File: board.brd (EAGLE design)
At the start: 76 x 83.5 mm, 82 parts, among them IC1 REG1117F, J1 LHBEAMOUT, J10 TEMP, J11 HORNOUT, J12 12V_SUPPLY, J13 STOPOUT, J14 TURNOUT, J15 FANOUT, J16 BLIGHTOUT, J17 AUXOUT, J18 AUX, J19 CAN, J2 BATT, J3 BLIGHT, J4 LHBEAM, J5 LRTURN, J6 WARNING, J7 HORN, J9 BREAK, Q1 FQD19N10LTM, Q2 FQD19N10LTM, Q3 FQD19N10LTM, Q4 IRF7424TRPBF, Q5 IRF7424TRPBF, Q6 IRF7424TRPBF, Q7 IRF7424TRPBF, Q8 IRF7424TRPBF, Q9 IRF7424TRPBF, U1 VOM1271T, U2 VOM1271T, U3 VOM1271T, U4 MC14504BDR2G, U5 MAX3051ESA+T

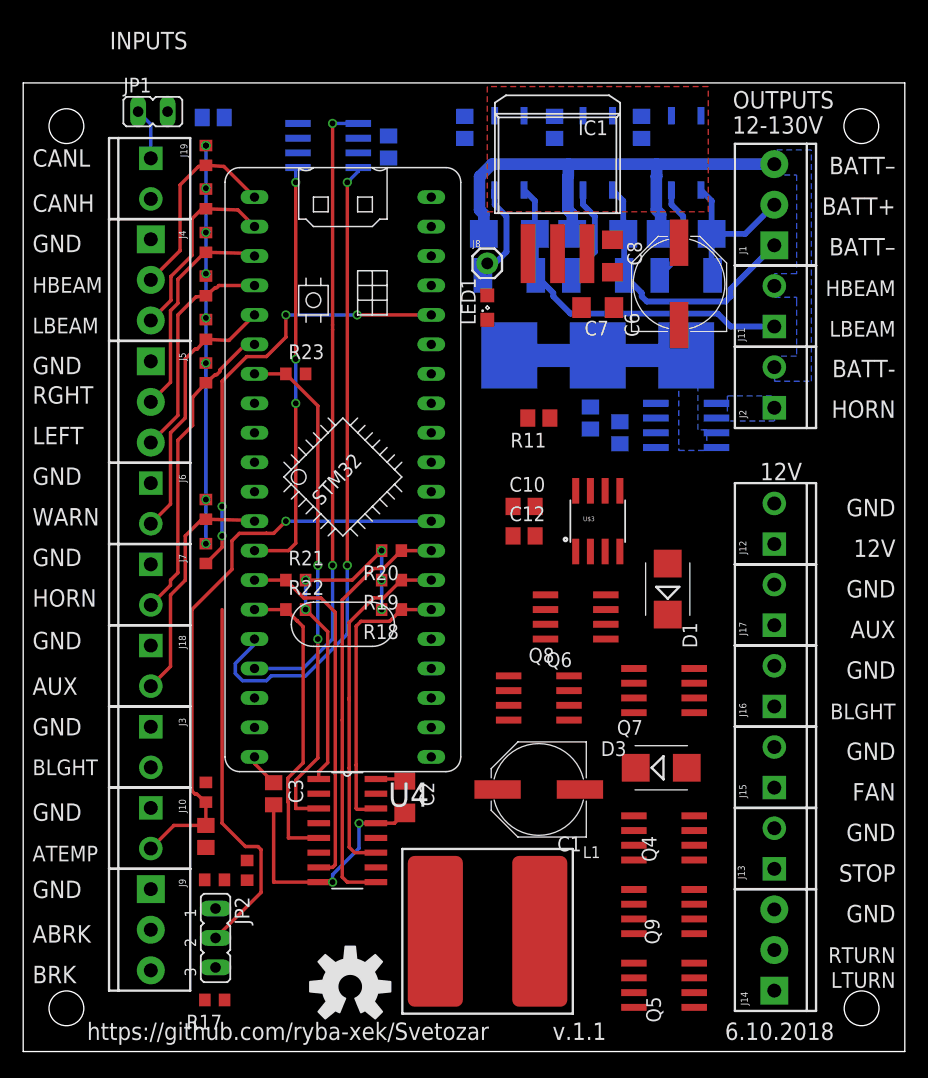
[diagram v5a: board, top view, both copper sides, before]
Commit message: Board v2, firmware is still WIP
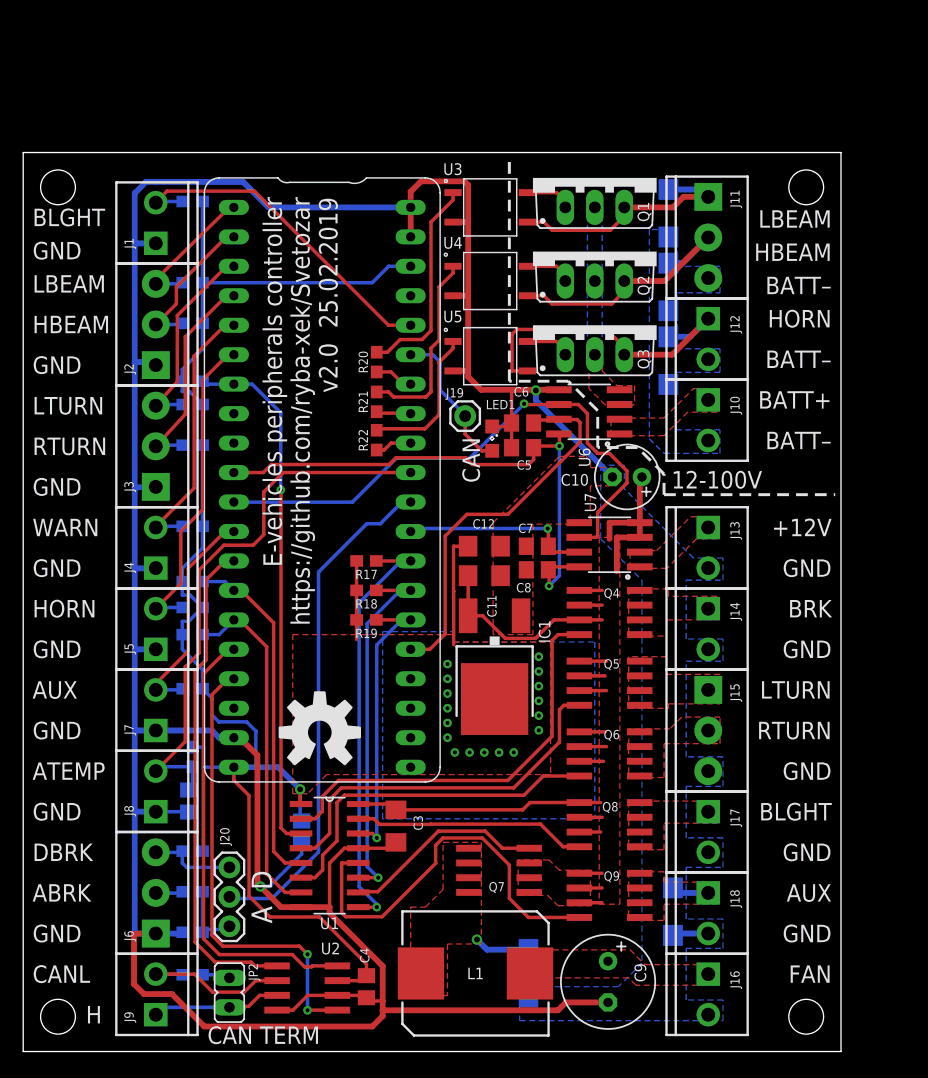
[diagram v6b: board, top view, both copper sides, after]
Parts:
- removed D6: STTH4R02UY, diode:SMB
- removed JP1: (no value), jumper:JP1
- removed LOGO2: OSHW-LOGOL, SparkFun-Aesthetics:OSHW-LOGO-L
- removed R23: 10k, rcl:R0603
- removed U$2, U$3: ACS711LC, svetozar:SO08
- added D2: ES1D, diode:DO214AC
- added J20: 455-1750-1-ND, SparkFun-Connectors:1X03
- added LOGO1: OSHW-LOGOL, SparkFun-Aesthetics:OSHW-LOGO-L
- added U6: ACS711KLCTR-12AB-T, svetozar:SO08
- added U7: ACS711ELCTR-25AB-T, svetozar:SO08
- C1: value 470u -> 0.1u; device rcl:PANASONIC_F -> rcl:C0805
- C10: value 1n -> 220u; device rcl:C0805 -> rcl:E2,5-6
- C11: value 0.1u -> 22u; device rcl:C0805 -> rcl:C1206
- C12: value 0.1u -> 47u; device rcl:C0805 -> rcl:C1206
- C2: device rcl:C1206 -> rcl:C0805
- C3: device rcl:C0805 -> rcl:C1206
- C6: value 470u -> 1n; device rcl:PANASONIC_F -> rcl:C0805
- C7: value 47u6V -> 1n; device rcl:C1206 -> rcl:C0805
- C8: value 22u16V -> 0.1u; device rcl:C1206 -> rcl:C0805
- C9: value 1n -> 470u; device rcl:C0805 -> rcl:E3,5-8
- D1, D3, D4, D5: value STTH4R02UY -> ES1D; device diode:SMB -> diode:DO214AC
- IC1: value REG1117F -> LD1117V33; device burr-brown:DD-3 -> v-reg:DPACK
- J1: value LHBEAMOUT -> BLIGHT; device SparkFun-Connectors:SCREWTERMINAL-3.5MM-3 -> SparkFun-Connectors:SCREWTERMINAL-3.5MM-2
- J10: value TEMP -> BATT
- J11: value HORNOUT -> LHBEAMOUT; device SparkFun-Connectors:SCREWTERMINAL-3.5MM-2 -> SparkFun-Connectors:SCREWTERMINAL-3.5MM-3
- J12: value 12V_SUPPLY -> HORHOUT
- J13: value STOPOUT -> 12V_SUPPLY
- J14: value TURNOUT -> STOPOUT; device SparkFun-Connectors:SCREWTERMINAL-3.5MM-3 -> SparkFun-Connectors:SCREWTERMINAL-3.5MM-2
- J15: value FANOUT -> TURNOUT; device SparkFun-Connectors:SCREWTERMINAL-3.5MM-2 -> SparkFun-Connectors:SCREWTERMINAL-3.5MM-3
- J16: value BLIGHTOUT -> FANOUT
- J17: value AUXOUT -> BLIGHTOUT
- J18: value AUX -> AUXOUT
- J19: value CAN -> (none); device SparkFun-Connectors:SCREWTERMINAL-3.5MM-2 -> SparkFun-Connectors:1X01
- J2: value BATT -> LHBEAM; device SparkFun-Connectors:SCREWTERMINAL-3.5MM-2 -> SparkFun-Connectors:SCREWTERMINAL-3.5MM-3
- J3: value BLIGHT -> LRTURN; device SparkFun-Connectors:SCREWTERMINAL-3.5MM-2 -> SparkFun-Connectors:SCREWTERMINAL-3.5MM-3
- J4: value LHBEAM -> WARN; device SparkFun-Connectors:SCREWTERMINAL-3.5MM-3 -> SparkFun-Connectors:SCREWTERMINAL-3.5MM-2
- J5: value LRTURN -> HORN; device SparkFun-Connectors:SCREWTERMINAL-3.5MM-3 -> SparkFun-Connectors:SCREWTERMINAL-3.5MM-2
- J6: value WARNING -> BREAK; device SparkFun-Connectors:SCREWTERMINAL-3.5MM-2 -> SparkFun-Connectors:SCREWTERMINAL-3.5MM-3
- J7: value HORN -> AUX
- J8: value (none) -> TEMP; device SparkFun-Connectors:1X01 -> SparkFun-Connectors:SCREWTERMINAL-3.5MM-2
- J9: value BREAK -> CAN; device SparkFun-Connectors:SCREWTERMINAL-3.5MM-3 -> SparkFun-Connectors:SCREWTERMINAL-3.5MM-2
- JP2: device jumper:JP2 -> jumper:JP1
- L1: value 15uH -> SRP1040-150M; device inductor-bourns:SDR1307 -> inductor-bourns:SRP1040
- Q1, Q2, Q3: value FQD19N10LTM -> PHP20NQ20T; device SparkFun-DiscreteSemi:DPAK -> transistor-power:TO220BV
- Q4, Q5, Q6, Q7, Q8, Q9: value IRF7424TRPBF -> (none)
- R1, R2, R3: value 160 -> 1K; device rcl:R0805 -> SparkFun-Resistors:0603
- R10, R17: value 1k -> 10K; device rcl:R0603 -> SparkFun-Resistors:0603
- R11: value 1k -> 1K; device rcl:R0805 -> SparkFun-Resistors:0603
- R12: value 1k -> 2.4K; device rcl:R0603 -> SparkFun-Resistors:0603
- R13: value 3k -> 120; device rcl:R0603 -> SparkFun-Resistors:0603
- R14: value 2.4k -> 10K; device rcl:R0603 -> SparkFun-Resistors:0603
- R15, R18, R19: value 10k -> 10K; device rcl:R0603 -> SparkFun-Resistors:0603
- R16: value 120 -> 10K; device rcl:R0805 -> SparkFun-Resistors:0603
- R20, R21, R22: value 10k -> 1K; device rcl:R0603 -> SparkFun-Resistors:0603
- R4, R5, R6, R7, R8: value 1k -> 1K; device rcl:R0603 -> SparkFun-Resistors:0603
- R9: value 1k -> 3K; device rcl:R0603 -> SparkFun-Resistors:0603
- U$1: device BluePill:BLUE_PILL -> svetozar:BLUE_PILL
- U1: value VOM1271T -> MC14504BDR2G; device VOM1271T:SOIC254P695X242-4N -> MC14504BDR2G:SOIC127P600X175-16N
- U2: value VOM1271T -> MAX3051ESA+T; device VOM1271T:SOIC254P695X242-4N -> MAX3051ESA:SO-08
- U4: value MC14504BDR2G -> VOM1271T; device MC14504BDR2G:SOIC127P600X175-16N -> VOM1271T:SOIC254P695X242-4N
- U5: value MAX3051ESA+T -> VOM1271T; device MAX3051ESA:SO-08 -> VOM1271T:SOIC254P695X242-4N
- moved U2 79.1 mm to (24.5, 5.48), flipped to the top, turned to 90 degrees
- moved U1 64.8 mm to (26.4, 16.9), flipped to the top, turned to 0 degrees
- moved D4 64.0 mm to (43.6, 6.73), turned to 270 degrees
- moved J10 59.6 mm to (59.1, 56.2)
- moved D5 58.4 mm to (56.0, 12.1), turned to 270 degrees
- moved J8 55.2 mm to (11.4, 20.7), turned to 90 degrees
- moved J2 53.4 mm to (11.4, 59.2)
- moved J1 53.3 mm to (11.4, 69.7)
- moved J18 52.6 mm to (59.1, 13.7)
- moved U4 48.9 mm to (40.3, 66.4)
- moved R8 48.7 mm to (14.6, 17.3), flipped to the bottom, turned to 180 degrees
- moved R9 48.5 mm to (14.6, 13.8), flipped to the bottom, turned to 180 degrees
- moved R10 48.2 mm to (14.6, 10.3), flipped to the bottom, turned to 180 degrees
- moved C9 47.3 mm to (50.4, 6.01), flipped to the top
- moved R16 44.6 mm to (14.6, 35.9)
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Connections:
- removed net ABRK_S: JP2.2, U$1.P$31
- removed net BATT+IN: J2.1, U$2.1, U$2.2
- removed net CSENS1: C9.1, U$1.P$36, U$2.7
- removed net FAULT: R11.1, U$1.P$11, U$2.6, U$3.6
- removed net HV1CTL: R1.1, U$1.P$28
- removed net HV1CTLG: R1.2, U1.1
- removed net HV1G: Q1.1, U1.4
- removed net HV2CTL: R2.1, U$1.P$27
- removed net HV2CTLG: R2.2, U2.1
- removed net HV2G: Q2.1, U2.4
- removed net HV3CTL: R3.1, U$1.P$29
- removed net HV3CTLG: R3.2, U3.1
- removed net HV3G: Q3.1, U3.4
- removed net IATEMP: C4.1, J10.2, R14.2, U$1.P$32
- removed net IBLGHT: J3.2, R4.2, U$1.P$25
- removed net LV1G: Q8.4, U4.15
- removed net LV2G: Q7.4, U4.10
- removed net LV3G: Q6.4, U4.12
- removed net LV4G: Q4.4, U4.2
- removed net LV5G: Q9.4, U4.4
- removed net LV6G: Q5.4, U4.6
- removed net LVCTL6: R18.1, U$1.P$35, U4.14
- removed net N$17: D3.C, L1.1, Q6.5, Q6.6, Q6.7, Q6.8
- removed net N$29: J4.3, R6.2, U$1.P$2
- removed net N$30: J4.2, R5.2, U$1.P$1
- removed net N$31: J7.2, R10.2, U$1.P$6
- removed net N$32: J5.3, R8.2, U$1.P$4
- removed net N$33: J5.2, R7.2, U$1.P$3
- removed net N$35: J6.2, R9.2, U$1.P$5
- removed net N$5: J9.2, R13.1
- removed net N$6: J8.1, LED1.A, U$1.P$26
- removed net N$7: J12.1, U$3.1, U$3.2
- removed net N$8: C10.1, U$1.P$30, U$3.7
- new net 12V_IN: J13.1, U7.1, U7.2
- new net CANL: J9.2, R13.1, U2.6
- new net CS3V3: C5.2, C8.2, U$1.P$10, U6.8, U7.8
- new net CSFAULT: U$1.P$11, U6.6, U7.6
- new net CSHV: C6.2, U$1.P$36, U6.7
- new net CSLV: C7.2, U$1.P$32, U7.7
- new net FANPWM: D4.C, L1.2, Q7.5, Q7.6, Q7.7, Q7.8
- new net HV: Q1.D, Q2.D, Q3.D, U6.3, U6.4
- new net HVCTL0: R20.1, U$1.P$27
- new net HVCTL1: R21.1, U$1.P$28
- new net HVCTL2: R22.1, U$1.P$29
- new net IBLIGHT: J1.2, R1.1, U$1.P$25
- new net IBREAK: J20.2, U$1.P$31
- new net IHBEAM: J2.2, R3.1, U$1.P$2
- new net IHORN: J5.2, R7.1, U$1.P$6
- new net ILBEAM: J2.3, R2.1, U$1.P$1
- new net ILTURN: J3.3, R4.1, U$1.P$3
- new net IRTURN: J3.2, R5.1, U$1.P$4
- new net ITEMP: C1.1, J8.2, R12.1, U$1.P$30
- new net IWARN: J4.2, R6.1, U$1.P$5
- new net LED: J19.1, LED1.A, U$1.P$26
- new net LVCTL0: R14.1, U$1.P$7, U1.3
- new net LVG0: Q4.4, U1.2
- new net LVG1: Q5.4, U1.4
- new net LVG2: Q6.4, U1.6
- new net LVG3: Q7.4, U1.10
- new net LVG4: Q8.4, U1.15
- new net LVG5: Q9.4, U1.12
- new net N$10: Q1.G, U3.4
- new net N$11: R21.2, U4.1
- new net N$12: Q2.G, U4.4
- new net N$13: R22.2, U5.1
- new net N$14: Q3.G, U5.4
- net +12V: now also C10.+, C11.1, C3.2, U1.16, U7.3, U7.4; no longer C2.1, C6.+, C8.1, U$3.3, U$3.4, U4.16
- net +3V3: now also C12.1, C2.2, C4.2, IC1.4, R1.2, R12.2, R14.2, R15.2, R16.2, R17.2, R2.2, R3.2, R4.2, R5.2, R6.2, R7.2, R8.2, U1.1, U2.3; no longer C3.1, C5.1, C7.1, IC1.2, R10.1, R12.1, R14.1, R17.1, R20.2, R21.2, R22.2, R23.2, R4.1, R5.1, R6.1, R7.1, R8.1, R9.1, U4.1, U5.3
- net AUXOUT: now also D5.C, J18.1, Q9.5, Q9.6, Q9.7, Q9.8; no longer D1.C, J17.1, Q8.5, Q8.6, Q8.7, Q8.8
- net BATT+: now also J10.1, U6.1, U6.2; no longer Q1.4, Q2.4, Q3.4, U$2.3, U$2.4
- net BATT-: now also D1.A, D2.A, D3.A, J10.2, J11.3, J12.2; no longer D4.A, D5.A, D6.A, J1.3, J11.2, J2.2
- net BLIGHTOUT: now also J17.1, Q8.5, Q8.6, Q8.7, Q8.8; no longer J16.1, Q7.5, Q7.6, Q7.7, Q7.8
- net CANH: now also J9.1, JP2.2, U2.7; no longer J19.2, R16.2, U5.7
- net CANRX: now also U2.4; no longer U5.4
- net CANSHDN: now also U2.5; no longer U5.5
- net CANTX: now also U2.1; no longer U5.1
- net FANOUT: now also C9.+, J16.1, L1.1; no longer C1.+, J15.1, L1.2
- net GND: now also C1.2, C10.-, C2.1, C3.1, C4.1, C5.1, C6.1, C7.1, C8.1, C9.-, D4.A, D5.A, J1.1, J14.2, J15.3, J18.2, J2.1, J8.1, R10.1, U1.13, U1.8, U2.8, U4.2, U6.5, U7.5; no longer C1.-, C10.2, C2.2, C3.2, C4.2, C5.2, C6.-, C7.2, C8.2, C9.2, D1.A, D3.A, J10.1, J12.2, J14.3, J15.2, J18.1, J9.1, R15.2, U$2.5, U$3.5, U1.2, U4.13, U4.8, U5.8
- net HBEAMOUT: now also D2.C, J11.2, Q2.S, U4.3; no longer D5.C, J1.2, Q2.3, U2.3
- net HORNOUT: now also D3.C, J12.1, Q3.S, U5.3; no longer D6.C, J11.1, Q3.3, U3.3
- net IAUX: now also J7.2, R11.1; no longer J18.2, R12.2
- net LBEAMOUT: now also D1.C, J11.1, Q1.S, U3.3; no longer D4.C, J1.1, Q1.3, U1.3
- net LTURNOUT: now also J15.1; no longer J14.1
- net LVCTL1: now also R15.1, U$1.P$14, U1.5; no longer R23.1, U$1.P$7, U4.3
- net LVCTL2: now also R16.1, U1.7; no longer R22.1, U4.5
- net LVCTL3: now also R17.1, U$1.P$33, U1.9; no longer R21.1, U$1.P$14, U4.7
- net LVCTL4: now also R18.1, U$1.P$34, U1.11; no longer R20.1, U$1.P$33, U4.9
- net LVCTL5: now also U$1.P$35, U1.14; no longer U$1.P$34, U4.11
- net N$1: now also J20.1, J6.3, R8.1; no longer JP1.2, R16.1
- net N$2: now also JP2.1, R13.2; no longer J19.1, JP1.1, U5.6
- net N$3: now also J20.3, R10.2, R9.2; no longer JP2.1, R13.2, R15.1
- net N$4: now also J6.2, R9.1; no longer J9.3, JP2.3, R17.2
- net N$9: now also R20.2, U3.1; no longer C11.1, C12.1, U$1.P$10, U$2.8, U$3.8
- net RTURNOUT: now also J15.2, Q6.5, Q6.6, Q6.7, Q6.8; no longer J14.2, Q9.5, Q9.6, Q9.7, Q9.8
- net STOPOUT: now also J14.1; no longer J13.1
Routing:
- net GND: track 22.6 -> 281.1 mm
- net +12V: track 2.54 -> 79.3 mm
- net +3V3: track 69.3 -> 143.7 mm, vias 14 -> 18
- net IATEMP: track 50.0 -> 0.00 mm, vias 1 -> 0
- net CSFAULT: track 0.00 -> 49.6 mm, vias 0 -> 1
- net ITEMP: track 0.00 -> 48.2 mm
- net CS3V3: track 0.00 -> 48.0 mm, vias 0 -> 2
- net LVCTL0: track 0.00 -> 45.7 mm, vias 0 -> 1
- net IBREAK: track 0.00 -> 44.0 mm
- net BATT-: track 43.3 -> 0.00 mm
- net IBLGHT: track 37.8 -> 0.00 mm, vias 4 -> 0
- net LVG0: track 0.00 -> 36.1 mm
- net LVG5: track 0.00 -> 34.6 mm
- net CSHV: track 0.00 -> 32.9 mm
- net LVG1: track 0.00 -> 32.4 mm
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- added copper zone on layer 1, net +12V
- added copper zone on layer 1, net +3V3
- added copper zone on layer 16, net +3V3
- added copper zone on layer 1, net 12V_IN
- added copper zone on layer 1, net AUXOUT
- added copper zone on layer 1, net BATT+
- added copper zone on layer 1, net BLIGHTOUT
- added copper zone on layer 1, net FANOUT
- added copper zone on layer 1, net FANPWM
- added copper zone on layer 1, net GND
- added copper zone on layer 16, net GND
- added copper zone on layer 1, net HV
- added copper zone on layer 16, net HV
- added copper zone on layer 1, net LTURNOUT
- added copper zone on layer 1, net RTURNOUT
- added copper zone on layer 1, net STOPOUT
- removed copper zone on layer 16, net BATT+
- removed copper zone on layer 16, net BATT+IN
- removed copper zone on layer 1, net HEATSINK
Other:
- board size 76 x 83.5 mm -> 70.5 x 77.5 mm
- board text added: "+12V"
- board text added: "12-100V"
- board text added: "A D"
- board text added: "CAN"
- board text added: "CAN TERM"
- board text added: "DBRK"
- board text added: "E-vehicles peripherals controller https://github.com/ryba-xek/Svetozar v2.0 25.02.2019"
- board text added: "H"
- board text removed: "12-130V"
- board text removed: "12V"
- board text removed: "6.10.2018"
- board text removed: "BATT-"
- board text removed: "CANH"
- board text removed: "INPUTS"
- board text removed: "LEFT"
- board text removed: "OUTPUTS"
- board text removed: "RGHT"
- board text removed: "STOP"
- board text removed: "https://github.com/ryba-xek/Svetozar"
- board text removed: "v.1.1"

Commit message: BOM for v2
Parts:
- C11: value 22u -> 22u 16V
- R20, R21, R22: value 1K -> 160
